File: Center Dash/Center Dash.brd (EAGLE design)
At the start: 159 x 86.7 mm, 90 parts, among them J1 502585-0470, Q1 BSS138, Q2 BSS138, Q3 BSS138, Q4 BSS138, U1 ADG3304BRUZ-REEL7, U2 TPS54540DDARQ1

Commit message: Update schematic to remove last spare
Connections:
- net SPARE_1 renamed SW_GS
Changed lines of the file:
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@@
 <wire x1="0" y1="69.977" x2="0" y2="57.15" width="0.3048" layer="1"/>
-</signal>
-<signal name="SPARE_1">
-<contactref element="U$2" pad="37/A18"/>
-<via x="13.716" y="77.978" extent="1-16" drill="0.3302"/>
-<wire x1="13.716" y1="77.978" x2="-16.764" y2="77.978" width="0.3048" layer="16"/>
-<wire x1="-16.764" y1="77.978" x2="-18.796" y2="75.946" width="0.3048" layer="16"/>
-<via x="-18.796" y="75.946" extent="1-16" drill="0.3302"/>
-<wire x1="-18.796" y1="75.946" x2="-18.796" y2="52.371" width="0.3048" layer="1"/>
-<wire x1="-18.796" y1="52.371" x2="-18.931" y2="52.236" width="0.3048" layer="1"/>
-<contactref element="U$1" pad="P$8"/>
-<wire x1="13.716" y1="77.978" x2="14" y2="77.694" width="0.3048" layer="1"/>
-<wire x1="14" y1="77.694" x2="14" y2="73.977" width="0.3048" layer="1"/>
 </signal>
 <signal name="N$11">
@@
 <wire x1="12" y1="69.937" x2="11.938" y2="69.875" width="0.3048" layer="1"/>
 </signal>
+<signal name="SW_GS">
+<contactref element="U$1" pad="P$8"/>
+<contactref element="U$2" pad="37/A18"/>
+<via x="13.716" y="77.978" extent="1-16" drill="0.3302"/>
+<wire x1="13.716" y1="77.978" x2="-16.764" y2="77.978" width="0.3048" layer="16"/>
+<wire x1="-16.764" y1="77.978" x2="-18.796" y2="75.946" width="0.3048" layer="16"/>
+<via x="-18.796" y="75.946" extent="1-16" drill="0.3302"/>
+<wire x1="-18.796" y1="75.946" x2="-18.796" y2="52.371" width="0.3048" layer="1"/>
+<wire x1="-18.796" y1="52.371" x2="-18.931" y2="52.236" width="0.3048" layer="1"/>
+<wire x1="13.716" y1="77.978" x2="14" y2="77.694" width="0.3048" layer="1"/>
+<wire x1="14" y1="77.694" x2="14" y2="73.977" width="0.3048" layer="1"/>
+</signal>
 </signals>

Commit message: I dont remember
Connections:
- removed net N$1: LED2.3-GND
- net GND: now also LED2.3-GND
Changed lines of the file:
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@@
 <wire x1="-31.115" y1="70.993" x2="-32.879" y2="70.993" width="0.3048" layer="16"/>
 <wire x1="-32.879" y1="70.993" x2="-33.136" y2="71.25" width="0.3048" layer="16"/>
+<contactref element="LED2" pad="3-GND"/>
 </signal>
 <signal name="+15V">
@@
 <wire x1="-60.833" y1="89.27170625" x2="-59.551025" y2="90.55368125" width="0.3048" layer="16"/>
 </signal>
-<signal name="N$1">
-<contactref element="LED2" pad="3-GND"/>
-</signal>
 <signal name="+3V3">

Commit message: Fixed Ignition 2
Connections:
- net IGNITION_2: now also U$2.20/A6
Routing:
- net IGNITION_2: track 66.5 -> 85.5 mm

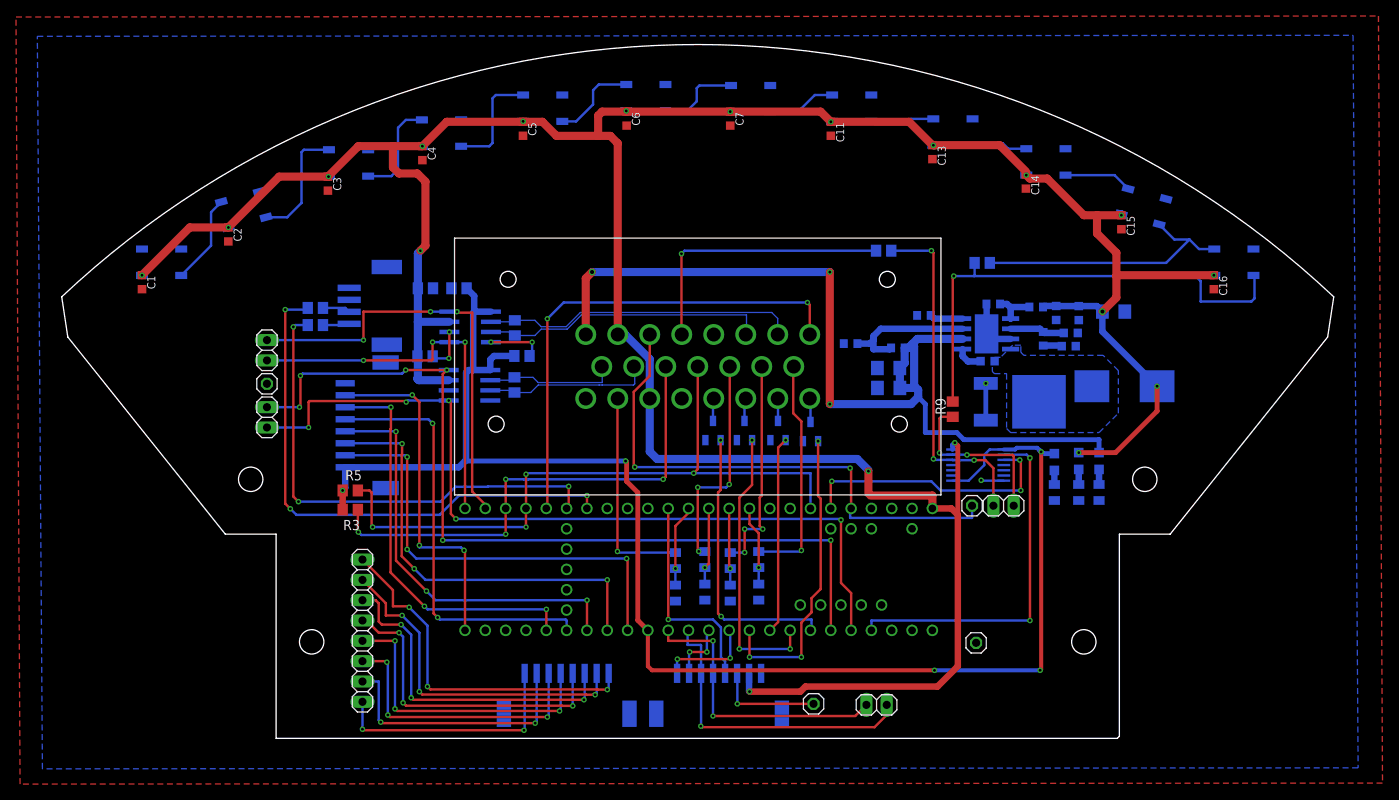
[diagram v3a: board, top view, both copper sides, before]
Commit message: Fixed two of the via overlaps
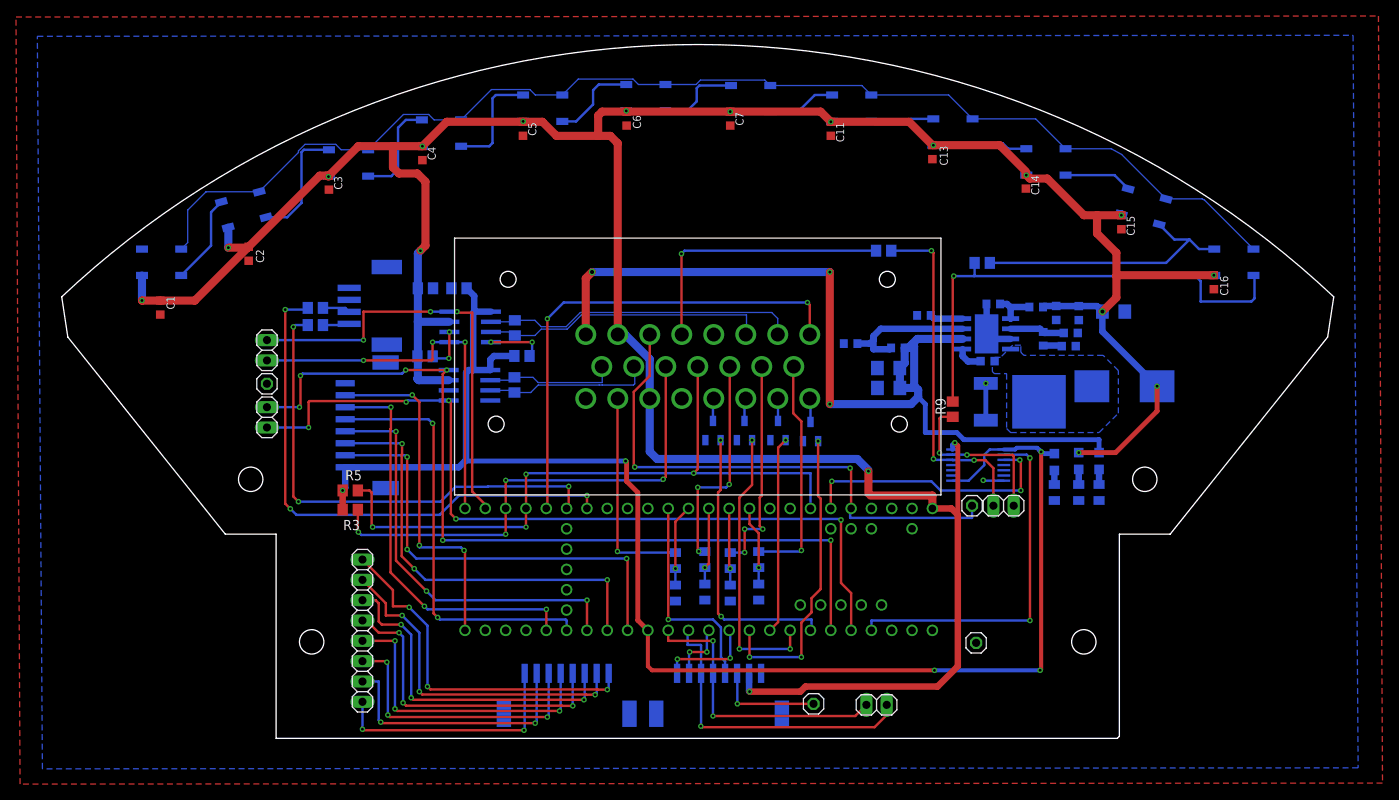
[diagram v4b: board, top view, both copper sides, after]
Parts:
- moved C1 3.91 mm to (-67.2, 77.3)
- moved C2 3.50 mm to (-56.1, 84.1)
- moved C3 0.18 mm to (-46.1, 93.0)
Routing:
- net GND: track 28.0 -> 183.0 mm
- net +5V: track 391.6 -> 399.2 mm
